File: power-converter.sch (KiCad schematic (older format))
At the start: 18 parts

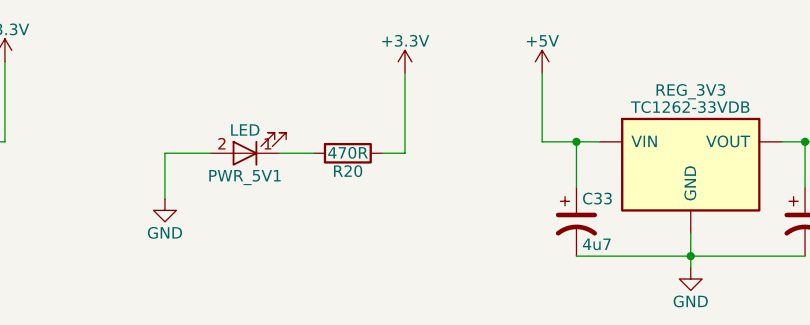
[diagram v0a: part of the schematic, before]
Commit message: Power leds
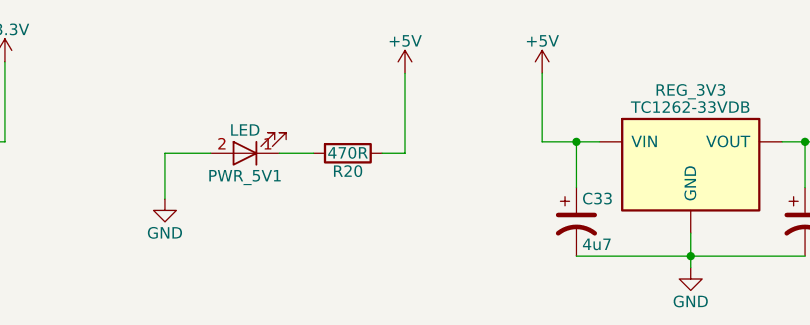
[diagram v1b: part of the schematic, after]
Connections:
- net +3V3: no longer R20.1
- net +5V: now also R20.1
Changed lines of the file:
@@
 	5750 3900 6150 3900
 $Comp
-L GND #PWR026
+L GND #PWR028
 U 1 1 5B2D2C35
 P 5000 3900
-F 0 "#PWR026" H 5000 3650 50  0001 C CNN
+F 0 "#PWR028" H 5000 3650 50  0001 C CNN
 F 1 "GND" H 5000 3750 50  0000 C CNN
 F 2 "" H 5000 3900 50  0001 C CNN
@@
 Connection ~ 8200 3900
 $Comp
-L GND #PWR027
+L GND #PWR029
 U 1 1 5B2D2C55
 P 7350 4400
-F 0 "#PWR027" H 7350 4150 50  0001 C CNN
+F 0 "#PWR029" H 7350 4150 50  0001 C CNN
 F 1 "GND" H 7350 4250 50  0000 C CNN
 F 2 "" H 7350 4400 50  0001 C CNN
@@
 $EndComp
 $Comp
-L GND #PWR028
+L GND #PWR030
 U 1 1 5B2D2C63
 P 8200 4400
-F 0 "#PWR028" H 8200 4150 50  0001 C CNN
+F 0 "#PWR030" H 8200 4150 50  0001 C CNN
 F 1 "GND" H 8200 4250 50  0000 C CNN
 F 2 "" H 8200 4400 50  0001 C CNN
@@
 	8200 4300 8200 4400
 $Comp
-L GND #PWR029
+L GND #PWR031
 U 1 1 5B2D2C6A
 P 6650 4300
-F 0 "#PWR029" H 6650 4050 50  0001 C CNN
+F 0 "#PWR031" H 6650 4050 50  0001 C CNN
 F 1 "GND" H 6650 4150 50  0000 C CNN
 F 2 "" H 6650 4300 50  0001 C CNN
@@
 	3850 3700 6150 3700
 $Comp
-L GND #PWR030
+L GND #PWR032
 U 1 1 5B2D2C79
 P 4200 4400
-F 0 "#PWR030" H 4200 4150 50  0001 C CNN
+F 0 "#PWR032" H 4200 4150 50  0001 C CNN
 F 1 "GND" H 4200 4250 50  0000 C CNN
 F 2 "" H 4200 4400 50  0001 C CNN
@@
 Connection ~ 6050 4300
 $Comp
-L +BATT #PWR031
+L +BATT #PWR033
 U 1 1 5B2D2CA5
 P 3850 3700
-F 0 "#PWR031" H 3850 3550 50  0001 C CNN
+F 0 "#PWR033" H 3850 3550 50  0001 C CNN
 F 1 "+BATT" H 3850 3840 50  0000 C CNN
 F 2 "" H 3850 3700 50  0001 C CNN
@@
 Connection ~ 4200 4250
 $Comp
-L +3.3V #PWR032
+L +3.3V #PWR034
 U 1 1 5B2DAE29
 P 3500 1350
-F 0 "#PWR032" H 3500 1200 50  0001 C CNN
+F 0 "#PWR034" H 3500 1200 50  0001 C CNN
 F 1 "+3.3V" H 3500 1490 50  0000 C CNN
 F 2 "" H 3500 1350 50  0001 C CNN
@@
 $EndComp
 $Comp
-L +3.3V #PWR033
+L +3.3V #PWR035
 U 1 1 5B2DAE36
 P 7300 1350
-F 0 "#PWR033" H 7300 1200 50  0001 C CNN
+F 0 "#PWR035" H 7300 1200 50  0001 C CNN
 F 1 "+3.3V" H 7300 1490 50  0000 C CNN
 F 2 "" H 7300 1350 50  0001 C CNN
@@
 $EndComp
 $Comp
-L GND #PWR034
+L GND #PWR036
 U 1 1 5B2DAE42
 P 6500 2250
-F 0 "#PWR034" H 6500 2000 50  0001 C CNN
+F 0 "#PWR036" H 6500 2000 50  0001 C CNN
 F 1 "GND" H 6500 2100 50  0000 C CNN
 F 2 "" H 6500 2250 50  0001 C CNN
@@
 $EndComp
 $Comp
-L GND #PWR035
+L GND #PWR037
 U 1 1 5B2DAE4F
 P 2450 1900
-F 0 "#PWR035" H 2450 1650 50  0001 C CNN
+F 0 "#PWR037" H 2450 1650 50  0001 C CNN
 F 1 "GND" H 2450 1750 50  0000 C CNN
 F 2 "" H 2450 1900 50  0001 C CNN
@@
 $EndComp
 $Comp
-L +5V #PWR036
+L +5V #PWR038
 U 1 1 5B114C95
 P 8650 3800
-F 0 "#PWR036" H 8650 3650 50  0001 C CNN
+F 0 "#PWR038" H 8650 3650 50  0001 C CNN
 F 1 "+5V" H 8650 3940 50  0000 C CNN
 F 2 "" H 8650 3800 50  0001 C CNN
@@
 	8650 3900 8650 3800
 $Comp
-L +5V #PWR037
+L +5V #PWR039
 U 1 1 5B115086
 P 5850 1400
-F 0 "#PWR037" H 5850 1250 50  0001 C CNN
+F 0 "#PWR039" H 5850 1250 50  0001 C CNN
 F 1 "+5V" H 5850 1540 50  0000 C CNN
 F 2 "" H 5850 1400 50  0001 C CNN
@@
 Wire Wire Line
 	3500 1700 3500 1350
-$Comp
-L +3.3V #PWR038
-U 1 1 5B16EDF6
-P 5250 1400
-F 0 "#PWR038" H 5250 1250 50  0001 C CNN
-F 1 "+3.3V" H 5250 1540 50  0000 C CNN
-F 2 "" H 5250 1400 50  0001 C CNN
-F 3 "" H 5250 1400 50  0001 C CNN
-	1    5250 1400
-	1    0    0    -1
-$EndComp
 $Comp
 L R R20
@@
 $EndComp
 $Comp
-L GND #PWR039
+L GND #PWR041
 U 1 1 5B16EE02
 P 4200 1950
-F 0 "#PWR039" H 4200 1700 50  0001 C CNN
+F 0 "#PWR041" H 4200 1700 50  0001 C CNN
 F 1 "GND" H 4200 1800 50  0000 C CNN
 F 2 "" H 4200 1950 50  0001 C CNN
@@
 Wire Wire Line
 	5250 1750 5250 1400
+$Comp
+L +5V #PWR?
+U 1 1 5B18DEB1
+P 5250 1400
+F 0 "#PWR?" H 5250 1250 50  0001 C CNN
+F 1 "+5V" H 5250 1540 50  0000 C CNN
+F 2 "" H 5250 1400 50  0001 C CNN
+F 3 "" H 5250 1400 50  0001 C CNN
+	1    5250 1400
+	1    0    0    -1
+$EndComp
 $EndSCHEMATC

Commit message: pcb layout
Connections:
- net +BATT: now also BATT-BUCK-PULLUP1.1; no longer BATT-BUCK-PULLUP1.2, TP-BATT-BUCK-ENABLE1.1
- net BATT-BUCK-ENABLE: now reaches BATT-BUCK1.5 (~ON~/OFF), JMP-BATT-BUCK-ENABLE1.1 (G1), SW_PWRON1.2 (B)
- net BATT-BUCK-ENABLE: now also BATT-BUCK-PULLUP1.2, TP-BATT-BUCK-ENABLE1.1; no longer BATT-BUCK-PULLUP1.1
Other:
- moved on the sheet: BATT-BUCK-PULLUP1
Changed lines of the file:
@@
 L R_Small BATT-BUCK-PULLUP1
 U 1 1 5B2D2C80
-P 5900 4100
-F 0 "BATT-BUCK-PULLUP1" H 5930 4120 50  0000 L CNN
-F 1 "10k" H 5930 4060 50  0000 L CNN
-F 2 "Resistors_SMD:R_0603" H 5900 4100 50  0001 C CNN
-F 3 "" H 5900 4100 50  0001 C CNN
-	1    5900 4100
-	1    0    0    -1
-$EndComp
-Wire Wire Line
-	5900 3900 5900 4000
+P 6050 4100
+F 0 "BATT-BUCK-PULLUP1" H 6080 4120 50  0000 L CNN
+F 1 "10k" H 6080 4060 50  0000 L CNN
+F 2 "Resistors_SMD:R_0603" H 6050 4100 50  0001 C CNN
+F 3 "" H 6050 4100 50  0001 C CNN
+	1    6050 4100
+	0    1    1    0
+$EndComp
+Wire Wire Line
+	5900 3900 5900 4500
 Connection ~ 5900 3900
-Wire Wire Line
-	5900 4200 5900 4500
 Text GLabel 5900 4500 3    60   Input ~ 0
 BATT-BUCK-ENABLE
@@
 Wire Wire Line
 	5900 4300 6500 4300
-Wire Wire Line
-	6050 4300 6050 3700
-Connection ~ 6050 3700
 Wire Wire Line
 	5800 3900 5800 4550
@@
 Wire Wire Line
 	6500 4300 6500 4550
-Connection ~ 6050 4300
 $Comp
 L +BATT #PWR033
@@
 $EndComp
 $Comp
-L GND #PWR041
+L GND #PWR040
 U 1 1 5B16EE02
 P 4200 1950
-F 0 "#PWR041" H 4200 1700 50  0001 C CNN
+F 0 "#PWR040" H 4200 1700 50  0001 C CNN
 F 1 "GND" H 4200 1800 50  0000 C CNN
 F 2 "" H 4200 1950 50  0001 C CNN
@@
 	5250 1750 5250 1400
 $Comp
-L +5V #PWR?
+L +5V #PWR041
 U 1 1 5B18DEB1
 P 5250 1400
-F 0 "#PWR?" H 5250 1250 50  0001 C CNN
+F 0 "#PWR041" H 5250 1250 50  0001 C CNN
 F 1 "+5V" H 5250 1540 50  0000 C CNN
 F 2 "" H 5250 1400 50  0001 C CNN
@@
 	1    0    0    -1
 $EndComp
+Connection ~ 5900 4100
+Wire Wire Line
+	6150 3700 6150 4100
+Wire Wire Line
+	5950 4100 5900 4100
 $EndSCHEMATC

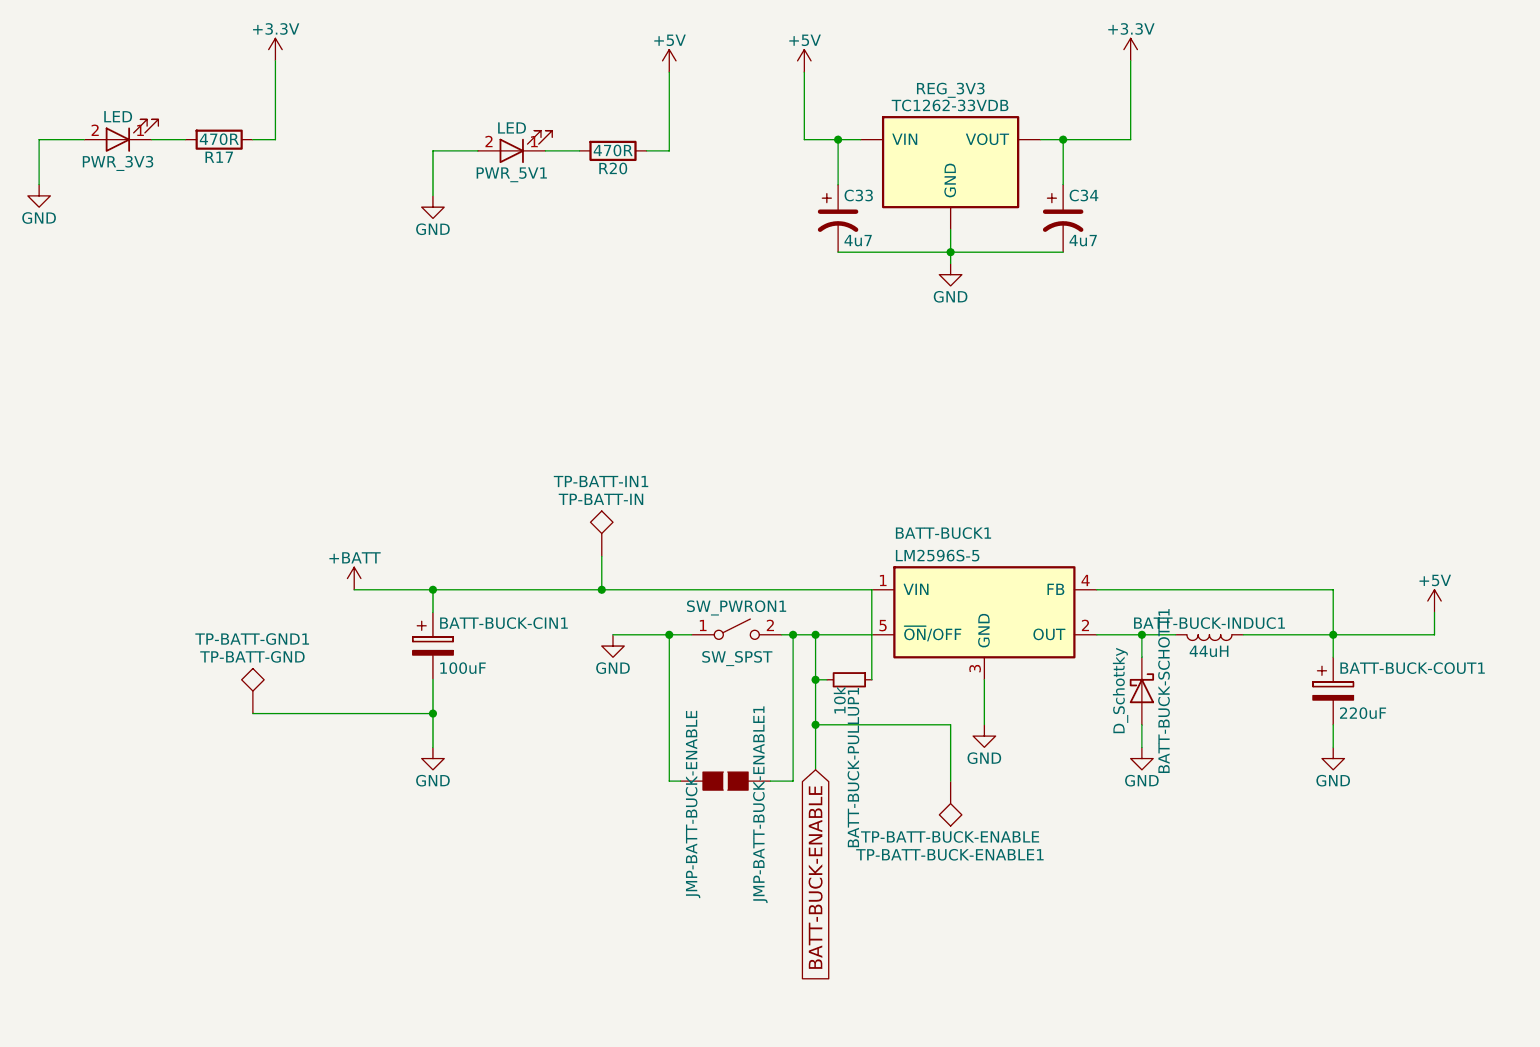
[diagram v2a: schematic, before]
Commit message: Changing tp silkscreen names
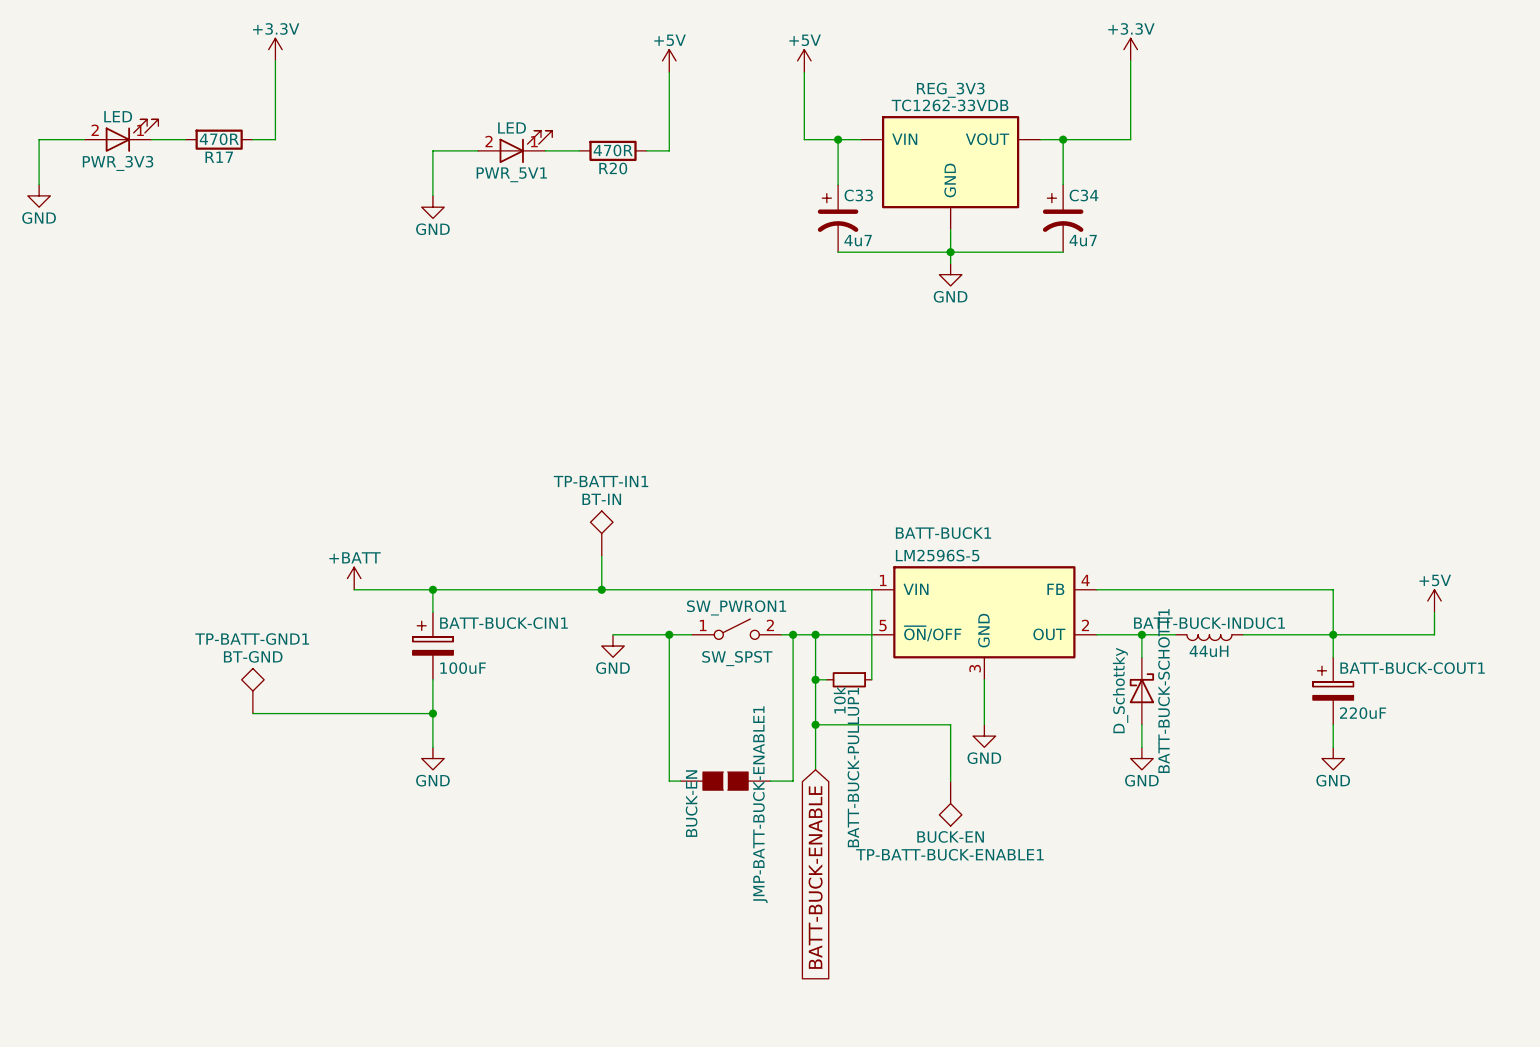
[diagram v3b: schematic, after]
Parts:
- JMP-BATT-BUCK-ENABLE1: value JMP-BATT-BUCK-ENABLE -> BUCK-EN
- TP-BATT-BUCK-ENABLE1: value TP-BATT-BUCK-ENABLE -> BUCK-EN
- TP-BATT-GND1: value TP-BATT-GND -> BT-GND
- TP-BATT-IN1: value TP-BATT-IN -> BT-IN
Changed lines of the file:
@@
 $Descr A4 11693 8268
 encoding utf-8
-Sheet 2 6
+Sheet 2 7
 Title "Power Converter"
 Date ""
@@
 	5750 3900 6150 3900
 $Comp
-L GND #PWR028
+L GND #PWR28
 U 1 1 5B2D2C35
 P 5000 3900
-F 0 "#PWR028" H 5000 3650 50  0001 C CNN
+F 0 "#PWR28" H 5000 3650 50  0001 C CNN
 F 1 "GND" H 5000 3750 50  0000 C CNN
 F 2 "" H 5000 3900 50  0001 C CNN
@@
 Connection ~ 8200 3900
 $Comp
-L GND #PWR029
+L GND #PWR34
 U 1 1 5B2D2C55
 P 7350 4400
-F 0 "#PWR029" H 7350 4150 50  0001 C CNN
+F 0 "#PWR34" H 7350 4150 50  0001 C CNN
 F 1 "GND" H 7350 4250 50  0000 C CNN
 F 2 "" H 7350 4400 50  0001 C CNN
@@
 $EndComp
 $Comp
-L GND #PWR030
+L GND #PWR35
 U 1 1 5B2D2C63
 P 8200 4400
-F 0 "#PWR030" H 8200 4150 50  0001 C CNN
+F 0 "#PWR35" H 8200 4150 50  0001 C CNN
 F 1 "GND" H 8200 4250 50  0000 C CNN
 F 2 "" H 8200 4400 50  0001 C CNN
@@
 	8200 4300 8200 4400
 $Comp
-L GND #PWR031
+L GND #PWR32
 U 1 1 5B2D2C6A
 P 6650 4300
-F 0 "#PWR031" H 6650 4050 50  0001 C CNN
+F 0 "#PWR32" H 6650 4050 50  0001 C CNN
 F 1 "GND" H 6650 4150 50  0000 C CNN
 F 2 "" H 6650 4300 50  0001 C CNN
@@
 	3850 3700 6150 3700
 $Comp
-L GND #PWR032
+L GND #PWR27
 U 1 1 5B2D2C79
 P 4200 4400
-F 0 "#PWR032" H 4200 4150 50  0001 C CNN
+F 0 "#PWR27" H 4200 4150 50  0001 C CNN
 F 1 "GND" H 4200 4250 50  0000 C CNN
 F 2 "" H 4200 4400 50  0001 C CNN
@@
 P 5500 4550
 F 0 "JMP-BATT-BUCK-ENABLE1" H 5600 4700 50  0000 C CNN
-F 1 "JMP-BATT-BUCK-ENABLE" H 5600 4401 50  0000 C CNN
+F 1 "BUCK-EN" H 5600 4401 50  0000 C CNN
 F 2 "Connect:GS2" V 5574 4550 50  0001 C CNN
 F 3 "" H 5500 4550 50  0001 C CNN
@@
 P 6500 4550
 F 0 "TP-BATT-BUCK-ENABLE1" H 6500 4850 50  0000 C BNN
-F 1 "TP-BATT-BUCK-ENABLE" H 6500 4800 50  0000 C CNN
+F 1 "BUCK-EN" H 6500 4800 50  0000 C CNN
 F 2 "Measurement_Points:Measurement_Point_Round-SMD-Pad_Small" H 6500 4550 50  0001 C CNN
 F 3 "" H 6500 4550 50  0001 C CNN
@@
 	6500 4300 6500 4550
 $Comp
-L +BATT #PWR033
+L +BATT #PWR25
 U 1 1 5B2D2CA5
 P 3850 3700
-F 0 "#PWR033" H 3850 3550 50  0001 C CNN
+F 0 "#PWR25" H 3850 3550 50  0001 C CNN
 F 1 "+BATT" H 3850 3840 50  0000 C CNN
 F 2 "" H 3850 3700 50  0001 C CNN
@@
 P 4950 3550
 F 0 "TP-BATT-IN1" H 4950 3850 50  0000 C BNN
-F 1 "TP-BATT-IN" H 4950 3800 50  0000 C CNN
+F 1 "BT-IN" H 4950 3800 50  0000 C CNN
 F 2 "Measurement_Points:Measurement_Point_Round-SMD-Pad_Small" H 4950 3550 50  0001 C CNN
 F 3 "" H 4950 3550 50  0001 C CNN
@@
 P 3400 4250
 F 0 "TP-BATT-GND1" H 3400 4550 50  0000 C BNN
-F 1 "TP-BATT-GND" H 3400 4500 50  0000 C CNN
+F 1 "BT-GND" H 3400 4500 50  0000 C CNN
 F 2 "Measurement_Points:Measurement_Point_Round-SMD-Pad_Small" H 3400 4250 50  0001 C CNN
 F 3 "" H 3400 4250 50  0001 C CNN
@@
 Connection ~ 4200 4250
 $Comp
-L +3.3V #PWR034
+L +3.3V #PWR24
 U 1 1 5B2DAE29
 P 3500 1350
-F 0 "#PWR034" H 3500 1200 50  0001 C CNN
+F 0 "#PWR24" H 3500 1200 50  0001 C CNN
 F 1 "+3.3V" H 3500 1490 50  0000 C CNN
 F 2 "" H 3500 1350 50  0001 C CNN
@@
 $EndComp
 $Comp
-L +3.3V #PWR035
+L +3.3V #PWR33
 U 1 1 5B2DAE36
 P 7300 1350
-F 0 "#PWR035" H 7300 1200 50  0001 C CNN
+F 0 "#PWR33" H 7300 1200 50  0001 C CNN
 F 1 "+3.3V" H 7300 1490 50  0000 C CNN
 F 2 "" H 7300 1350 50  0001 C CNN
@@
 $EndComp
 $Comp
-L GND #PWR036
+L GND #PWR31
 U 1 1 5B2DAE42
 P 6500 2250
-F 0 "#PWR036" H 6500 2000 50  0001 C CNN
+F 0 "#PWR31" H 6500 2000 50  0001 C CNN
 F 1 "GND" H 6500 2100 50  0000 C CNN
 F 2 "" H 6500 2250 50  0001 C CNN
@@
 $EndComp
 $Comp
-L GND #PWR037
+L GND #PWR23
 U 1 1 5B2DAE4F
 P 2450 1900
-F 0 "#PWR037" H 2450 1650 50  0001 C CNN
+F 0 "#PWR23" H 2450 1650 50  0001 C CNN
 F 1 "GND" H 2450 1750 50  0000 C CNN
 F 2 "" H 2450 1900 50  0001 C CNN
@@
 $EndComp
 $Comp
-L +5V #PWR038
+L +5V #PWR36
 U 1 1 5B114C95
 P 8650 3800
-F 0 "#PWR038" H 8650 3650 50  0001 C CNN
+F 0 "#PWR36" H 8650 3650 50  0001 C CNN
 F 1 "+5V" H 8650 3940 50  0000 C CNN
 F 2 "" H 8650 3800 50  0001 C CNN
@@
 	8650 3900 8650 3800
 $Comp
-L +5V #PWR039
+L +5V #PWR30
 U 1 1 5B115086
 P 5850 1400
-F 0 "#PWR039" H 5850 1250 50  0001 C CNN
+F 0 "#PWR30" H 5850 1250 50  0001 C CNN
 F 1 "+5V" H 5850 1540 50  0000 C CNN
 F 2 "" H 5850 1400 50  0001 C CNN
@@
 $EndComp
 $Comp
-L GND #PWR040
+L GND #PWR26
 U 1 1 5B16EE02
 P 4200 1950
-F 0 "#PWR040" H 4200 1700 50  0001 C CNN
+F 0 "#PWR26" H 4200 1700 50  0001 C CNN
 F 1 "GND" H 4200 1800 50  0000 C CNN
 F 2 "" H 4200 1950 50  0001 C CNN
@@
 	5250 1750 5250 1400
 $Comp
-L +5V #PWR041
+L +5V #PWR29
 U 1 1 5B18DEB1
 P 5250 1400
-F 0 "#PWR041" H 5250 1250 50  0001 C CNN
+F 0 "#PWR29" H 5250 1250 50  0001 C CNN
 F 1 "+5V" H 5250 1540 50  0000 C CNN
 F 2 "" H 5250 1400 50  0001 C CNN

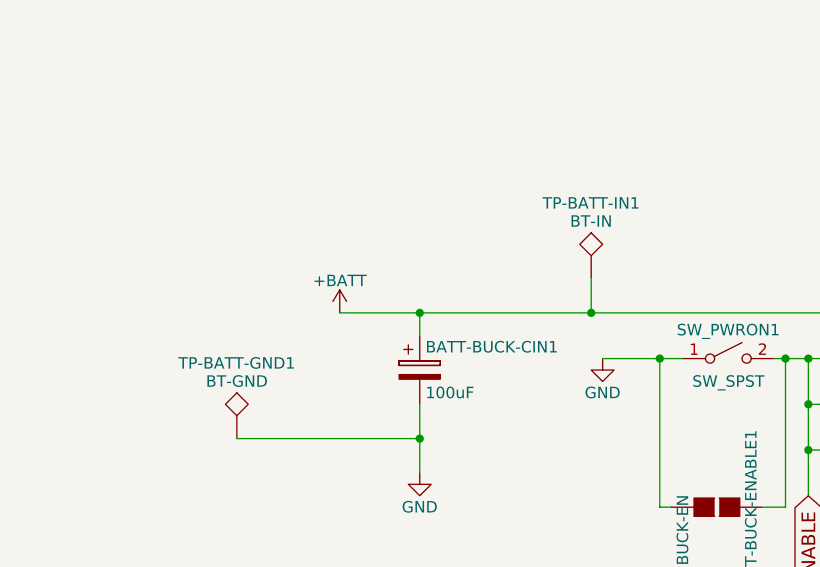
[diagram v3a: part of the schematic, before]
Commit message: tp name fixes
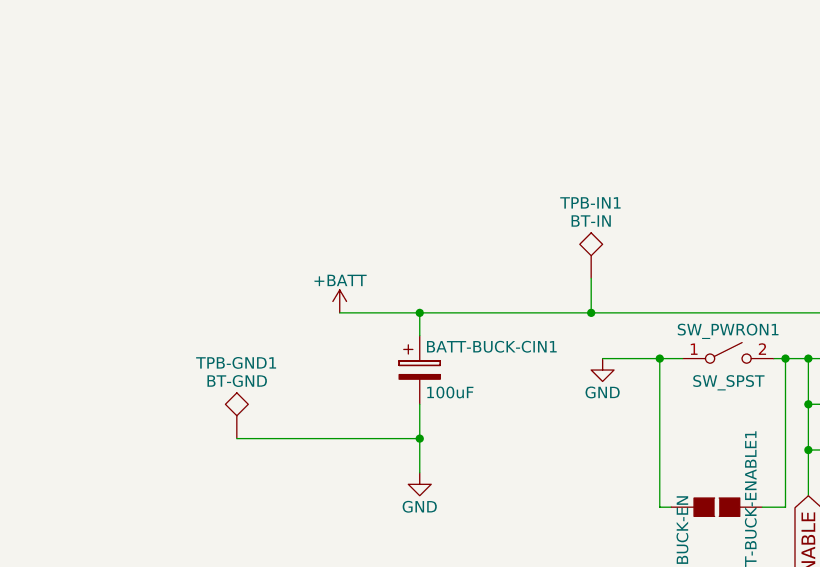
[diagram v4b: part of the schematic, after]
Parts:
- renumbered TP-BATT-GND1 to TPB-GND1, TP-BATT-IN1 to TPB-IN1
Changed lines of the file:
@@
 Connection ~ 4200 3700
 $Comp
-L TEST TP-BATT-IN1
+L TEST TPB-IN1
 U 1 1 5B2D2CAC
 P 4950 3550
-F 0 "TP-BATT-IN1" H 4950 3850 50  0000 C BNN
+F 0 "TPB-IN1" H 4950 3850 50  0000 C BNN
 F 1 "BT-IN" H 4950 3800 50  0000 C CNN
 F 2 "Measurement_Points:Measurement_Point_Round-SMD-Pad_Small" H 4950 3550 50  0001 C CNN
@@
 Connection ~ 4950 3700
 $Comp
-L TEST TP-BATT-GND1
+L TEST TPB-GND1
 U 1 1 5B2D2CB5
 P 3400 4250
-F 0 "TP-BATT-GND1" H 3400 4550 50  0000 C BNN
+F 0 "TPB-GND1" H 3400 4550 50  0000 C BNN
 F 1 "BT-GND" H 3400 4500 50  0000 C CNN
 F 2 "Measurement_Points:Measurement_Point_Round-SMD-Pad_Small" H 3400 4250 50  0001 C CNN
